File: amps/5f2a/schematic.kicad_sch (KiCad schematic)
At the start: 31 parts, among them T2 SE 5k:8

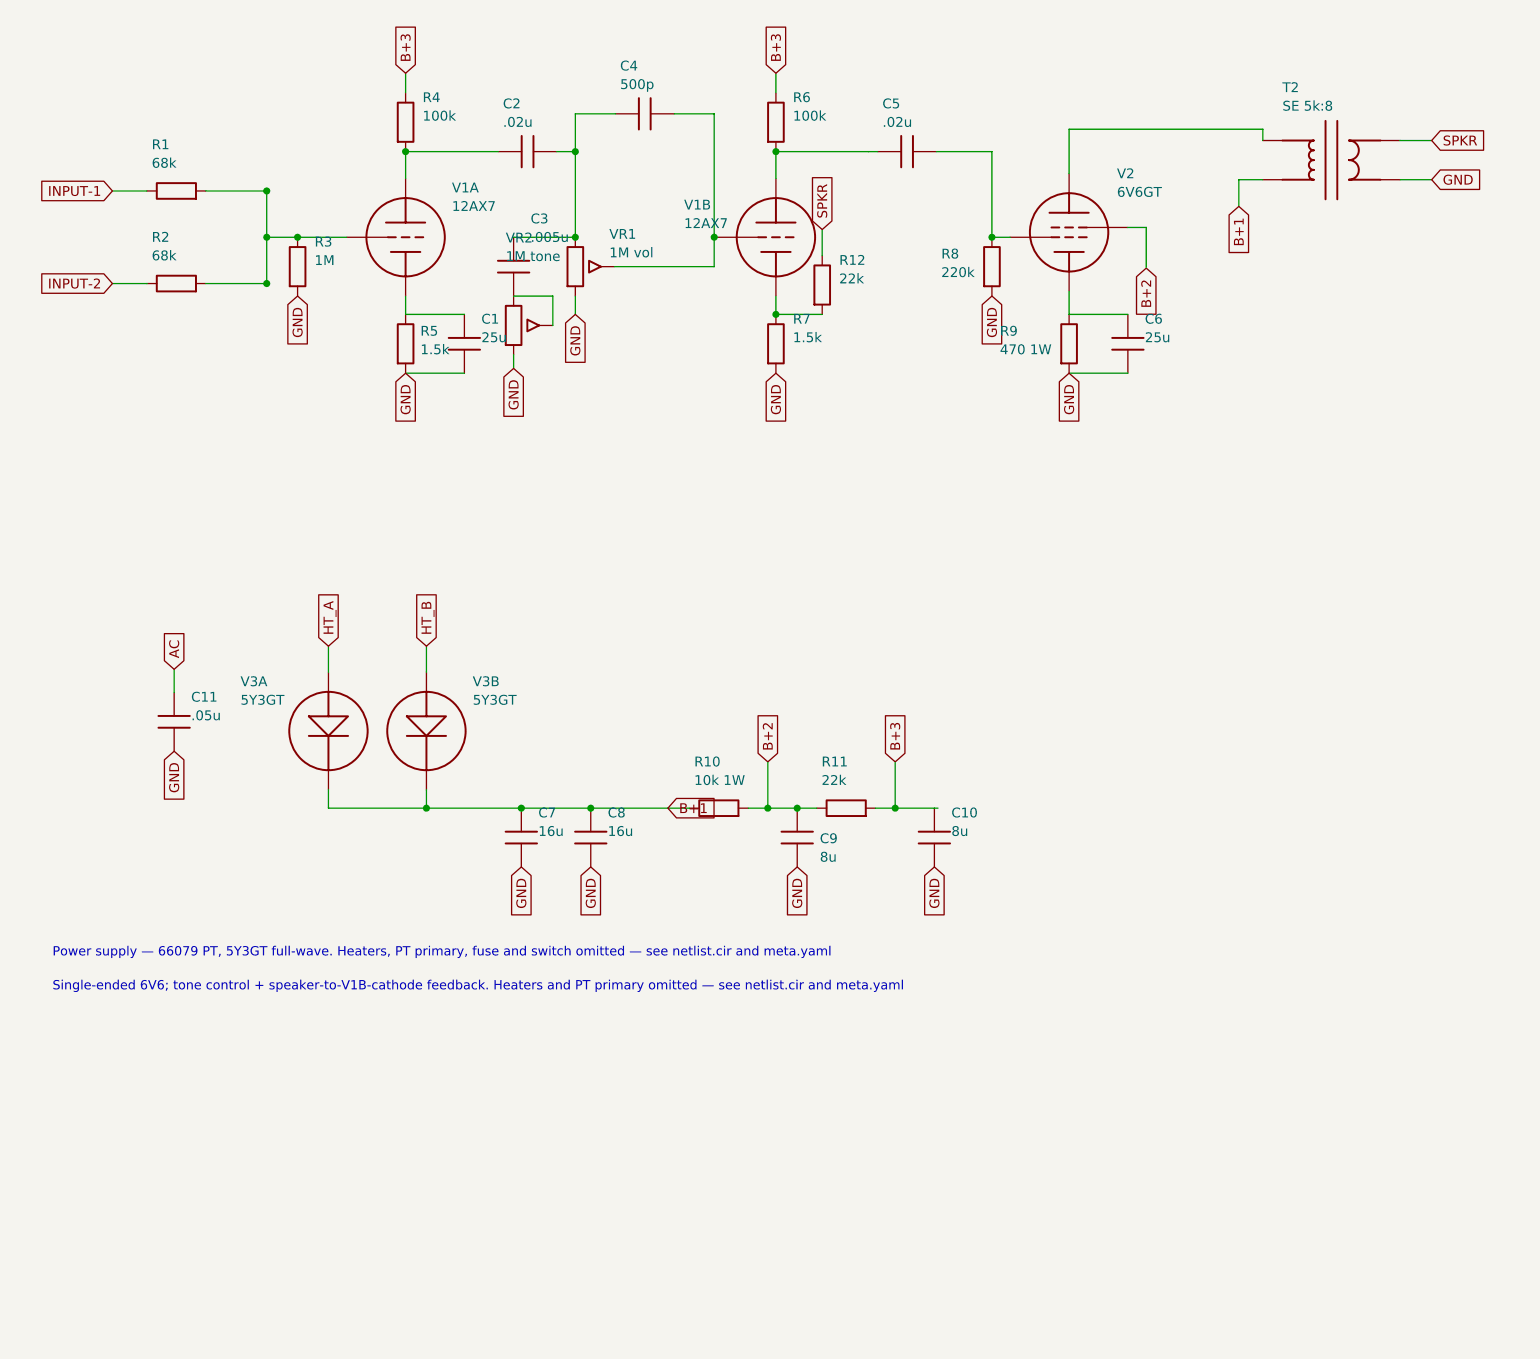
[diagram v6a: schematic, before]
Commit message: Add: real tube pin numbers and readable valve glyphs on every schematic
Phase B of the drawing program. A factory service sheet numbers every tube
pin, because the number is what a technician puts a probe on. This corpus
printed none, and the numbers hidden in its symbols were positional
placeholders (P=1, G=2, K=3) that would have published a 6V6GT's plate as
pin 1 when it is pin 3.

1055 electrodes now carry the real number, 1027 lettered (27 are shared
filaments deduped, 1 dropped for want of clear space on the 6G2). Resolved per
instance from reference/tubes/<slug>.yaml through the same alias resolution the
layout renderer uses, so a 12AX7 section and a 6SL7 section each get their own
basing. A valve whose basing the corpus does not carry prints nothing rather
than a wrong number.

Section letters and basing units are now separate things, which cost a detour
worth recording. The RCA 12AX7-A sheet reads "Pin 1 - Plate of Unit No.2 ...
Pin 6 - Plate of Unit No.1", so unit numbering is not pin order; the 5Y3 and
GZ34 number their units in opposite pin order, so nothing positional can
express it. But the section LETTER is a designator, not a basing fact: this
corpus, like every technician, calls the first stage in signal order V1A, and
five amps' prose already did. On four amps the factory sheets put that first
stage on the other half -- the AA764's own schematic prints +200 V on pin 1 --
so those drawings now state their unit explicitly, each citing its source, and
no letter, netlist, parts list or layout comment changed. 183 layout comments
agree with the printed numbers, 0 disagree. A guard fires if two halves of one
bottle resolve to the same unit, which is exactly how this was found.

Glyphs: the cathode gains a bracket and filament hairpin so it can no longer be
confused with the plate bar, the pentode's screen sits on its own row, and a
rectifier draws as one envelope over its sections instead of two apparent
bottles. Line weights are scaled per sheet to a co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
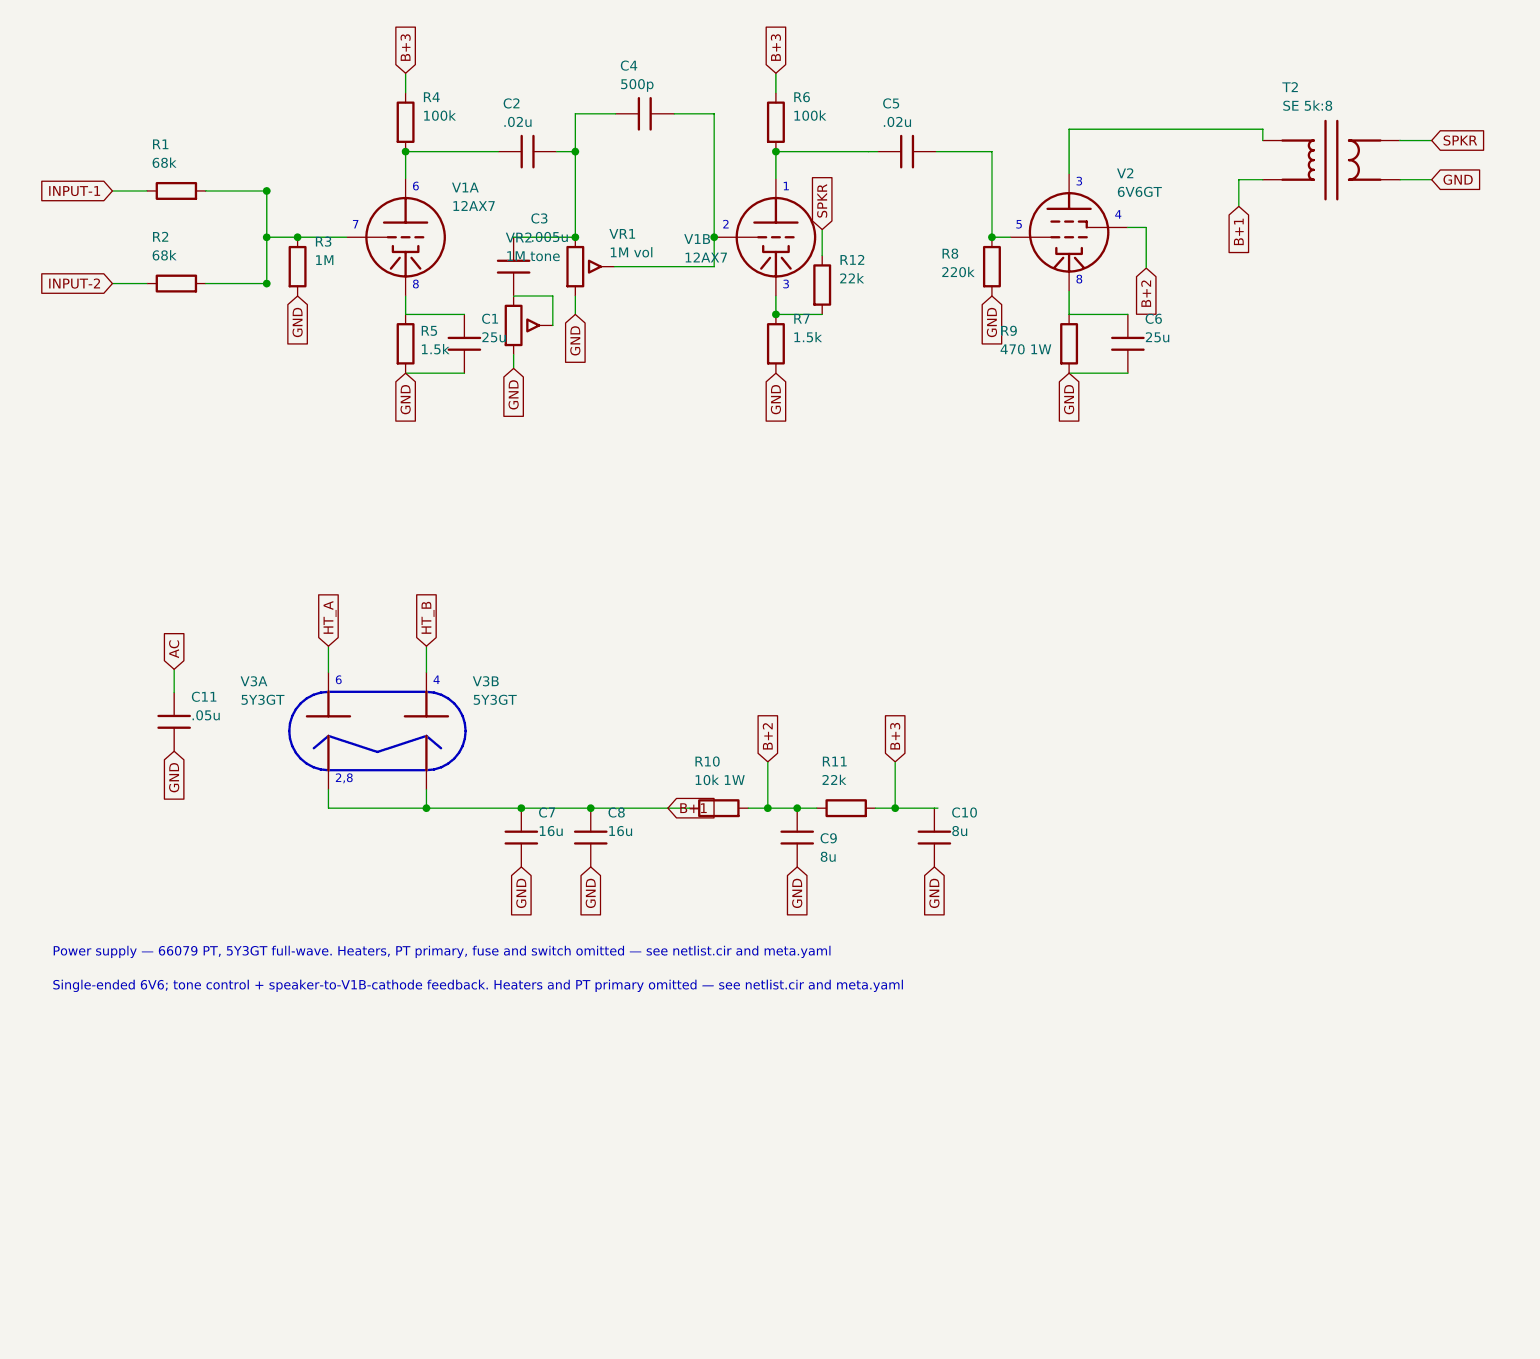
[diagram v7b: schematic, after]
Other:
- note added: "1"
- note added: "2"
- note added: "2,8"
- note added: "3"
- note added: "4"
- note added: "5"
- note added: "6"
- note added: "7"
- note added: "8"
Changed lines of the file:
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@@
   (wire (pts (xy 40.4724 38.278) (xy 40.4724 44.278))
     (stroke (width 0) (type default)))
-  (junction (at 40.4724 32.278) (diameter 0) (color 0 0 0 0))
-  (junction (at 40.4724 44.278) (diameter 0) (color 0 0 0 0))
-  (junction (at 40.4724 38.278) (diameter 0) (color 0 0 0 0))
+  (junction (at 40.4724 32.278) (diameter 1) (color 0 0 0 0))
+  (junction (at 40.4724 44.278) (diameter 1) (color 0 0 0 0))
+  (junction (at 40.4724 38.278) (diameter 1) (color 0 0 0 0))
   (wire (pts (xy 40.4724 38.278) (xy 44.4724 38.278))
     (stroke (width 0) (type default)))
-  (junction (at 44.4724 38.278) (diameter 0) (color 0 0 0 0))
+  (junction (at 44.4724 38.278) (diameter 1) (color 0 0 0 0))
   (symbol (lib_id "cx:R") (at 44.4724 42.088 0) (unit 1)
     (in_bom yes) (on_board yes)
@@
   (wire (pts (xy 58.4724 27.178) (xy 70.4724 27.178))
     (stroke (width 0) (type default)))
-  (junction (at 58.4724 27.178) (diameter 0) (color 0 0 0 0))
+  (junction (at 58.4724 27.178) (diameter 1) (color 0 0 0 0))
   (symbol (lib_id "cx:C") (at 74.2824 27.178 90) (unit 1)
     (in_bom yes) (on_board yes)
@@
   (wire (pts (xy 80.4724 27.178) (xy 80.4724 38.278))
     (stroke (width 0) (type default)))
-  (junction (at 80.4724 27.178) (diameter 0) (color 0 0 0 0))
-  (junction (at 80.4724 38.278) (diameter 0) (color 0 0 0 0))
+  (junction (at 80.4724 27.178) (diameter 1) (color 0 0 0 0))
+  (junction (at 80.4724 38.278) (diameter 1) (color 0 0 0 0))
   (symbol (lib_id "cx:POT") (at 80.4724 42.088 0) (unit 1)
     (in_bom yes) (on_board yes)
@@
   (wire (pts (xy 98.4724 22.278) (xy 98.4724 38.278))
     (stroke (width 0) (type default)))
-  (junction (at 98.4724 38.278) (diameter 0) (color 0 0 0 0))
+  (junction (at 98.4724 38.278) (diameter 1) (color 0 0 0 0))
   (wire (pts (xy 80.4724 38.278) (xy 72.4724 38.278))
     (stroke (width 0) (type default)))
@@
   (symbol (lib_id "cx:TRIODE") (at 106.472 38.278 0) (unit 1)
     (in_bom yes) (on_board yes)
-    (property "Reference" "V1B" (at 94.5678 34.098 0) (effects (font (size 1.27 1.27)) (justify left)))
-    (property "Value" "12AX7" (at 94.5678 36.498 0) (effects (font (size 1.27 1.27)) (justify left))))
+    (property "Reference" "V1B" (at 94.5678 38.558 0) (effects (font (size 1.27 1.27)) (justify left)))
+    (property "Value" "12AX7" (at 94.5678 40.958 0) (effects (font (size 1.27 1.27)) (justify left))))
   (wire (pts (xy 98.4724 38.278) (xy 98.8524 38.278))
     (stroke (width 0) (type default)))
   (wire (pts (xy 106.472 45.898) (xy 106.472 48.278))
     (stroke (width 0) (type default)))
-  (junction (at 106.472 48.278) (diameter 0) (color 0 0 0 0))
+  (junction (at 106.472 48.278) (diameter 1) (color 0 0 0 0))
   (symbol (lib_id "cx:R") (at 106.472 52.088 0) (unit 1)
     (in_bom yes) (on_board yes)
@@
   (wire (pts (xy 106.472 27.178) (xy 118.472 27.178))
     (stroke (width 0) (type default)))
-  (junction (at 106.472 27.178) (diameter 0) (color 0 0 0 0))
+  (junction (at 106.472 27.178) (diameter 1) (color 0 0 0 0))
   (symbol (lib_id "cx:C") (at 123.472 27.178 90) (unit 1)
     (in_bom yes) (on_board yes)
@@
   (wire (pts (xy 134.472 38.278) (xy 136.852 38.278))
     (stroke (width 0) (type default)))
-  (junction (at 134.472 38.278) (diameter 0) (color 0 0 0 0))
+  (junction (at 134.472 38.278) (diameter 1) (color 0 0 0 0))
   (symbol (lib_id "cx:R") (at 134.472 42.088 0) (unit 1)
     (in_bom yes) (on_board yes)
@@
   (wire (pts (xy 82.4724 112.278) (xy 92.4724 112.278))
     (stroke (width 0) (type default)))
-  (junction (at 61.1724 112.278) (diameter 0) (color 0 0 0 0))
-  (junction (at 73.4724 112.278) (diameter 0) (color 0 0 0 0))
+  (junction (at 61.1724 112.278) (diameter 1) (color 0 0 0 0))
+  (junction (at 73.4724 112.278) (diameter 1) (color 0 0 0 0))
   (symbol (lib_id "cx:C") (at 73.4724 116.088 0) (unit 1)
     (in_bom yes) (on_board yes)
@@
   (global_label "GND" (shape input) (at 73.4724 119.898 270)
     (effects (font (size 1.27 1.27)) (justify right)))
-  (junction (at 82.4724 112.278) (diameter 0) (color 0 0 0 0))
+  (junction (at 82.4724 112.278) (diameter 1) (color 0 0 0 0))
   (symbol (lib_id "cx:C") (at 82.4724 116.088 0) (unit 1)
     (in_bom yes) (on_board yes)
@@
     (property "Reference" "R10" (at 95.8724 106.278 270) (effects (font (size 1.27 1.27)) (justify left)))
     (property "Value" "10k 1W" (at 95.8724 108.678 270) (effects (font (size 1.27 1.27)) (justify left))))
-  (junction (at 105.422 112.278) (diameter 0) (color 0 0 0 0))
+  (junction (at 105.422 112.278) (diameter 1) (color 0 0 0 0))
   (global_label "B+2" (shape input) (at 105.422 106.278 90)
     (effects (font (size 1.27 1.27)) (justify left)))
   (wire (pts (xy 105.422 106.278) (xy 105.422 112.278))
     (stroke (width 0) (type default)))
-  (junction (at 109.232 112.278) (diameter 0) (color 0 0 0 0))
+  (junction (at 109.232 112.278) (diameter 1) (color 0 0 0 0))
   (symbol (lib_id "cx:C") (at 109.232 116.088 0) (unit 1)
     (in_bom yes) (on_board yes)
@@
   (wire (pts (xy 127.012 112.278) (xy 127.472 112.278))
     (stroke (width 0) (type default)))
-  (junction (at 121.932 112.278) (diameter 0) (color 0 0 0 0))
+  (junction (at 121.932 112.278) (diameter 1) (color 0 0 0 0))
   (global_label "B+3" (shape input) (at 121.932 106.278 90)
     (effects (font (size 1.27 1.27)) (justify left)))
@@
   (global_label "GND" (shape input) (at 127.012 119.898 270)
     (effects (font (size 1.27 1.27)) (justify right)))
+  (polyline (pts (xy 61.1724 97.198) (xy 62.1634 97.296) (xy 63.1164 97.585) (xy 63.9944 98.054) (xy 64.7644 98.686) (xy 65.3964 99.456) (xy 65.8654 100.334) (xy 66.1544 101.287) (xy 66.2524 102.278) (xy 66.1544 103.269) (xy 65.8654 104.222) (xy 65.3964 105.1) (xy 64.7644 105.87) (xy 63.9944 106.502) (xy 63.1164 106.971) (xy 62.1634 107.26) (xy 61.1724 107.358) (xy 48.4724 107.358) (xy 47.4814 107.26) (xy 46.5284 106.971) (xy 45.6504 106.502) (xy 44.8804 105.87) (xy 44.2484 105.1) (xy 43.7794 104.222) (xy 43.4904 103.269) (xy 43.3924 102.278) (xy 43.4904 101.287) (xy 43.7794 100.334) (xy 44.2484 99.456) (xy 44.8804 98.686) (xy 45.6504 98.054) (xy 46.5284 97.585) (xy 47.4814 97.296) (xy 48.4724 97.198) (xy 61.1724 97.198))
+    (stroke (width 0.3) (type default) (color 197 163 255 1)) (fill (type none)))
+  (polyline (pts (xy 46.5724 104.513) (xy 48.4724 102.913) (xy 54.8224 104.993) (xy 61.1724 102.913) (xy 63.0724 104.513))
+    (stroke (width 0.3) (type default) (color 197 163 255 1)) (fill (type none)))
+  (text "6" (at 59.3224 31.928 0)
+    (effects (font (size 1.1 1.1)) (justify left)))
+  (text "7" (at 51.5252 36.878 0)
+    (effects (font (size 1.1 1.1)) (justify left)))
+  (text "8" (at 59.3224 44.628 0)
+    (effects (font (size 1.1 1.1)) (justify left)))
+  (text "1" (at 107.322 31.928 0)
+    (effects (font (size 1.1 1.1)) (justify left)))
+  (text "2" (at 99.5252 36.878 0)
+    (effects (font (size 1.1 1.1)) (justify left)))
+  (text "3" (at 107.322 44.628 0)
+    (effects (font (size 1.1 1.1)) (justify left)))
+  (text "3" (at 145.322 31.293 0)
+    (effects (font (size 1.1 1.1)) (justify left)))
+  (text "5" (at 137.525 36.878 0)
+    (effects (font (size 1.1 1.1)) (justify left)))
+  (text "4" (at 150.372 35.608 0)
+    (effects (font (size 1.1 1.1)) (justify left)))
+  (text "8" (at 145.322 43.993 0)
+    (effects (font (size 1.1 1.1)) (justify left)))
+  (text "6" (at 49.3224 95.928 0)
+    (effects (font (size 1.1 1.1)) (justify left)))
+  (text "2,8" (at 49.3224 108.628 0)
+    (effects (font (size 1.1 1.1)) (justify left)))
+  (text "4" (at 62.0224 95.928 0)
+    (effects (font (size 1.1 1.1)) (justify left)))
   (text "Power supply — 66079 PT, 5Y3GT full-wave. Heaters, PT primary, fuse and switch omitted — see netlist.cir and meta.yaml" (at 12.7 131.056 0)
     (effects (font (size 1.2 1.2)) (justify left)))
